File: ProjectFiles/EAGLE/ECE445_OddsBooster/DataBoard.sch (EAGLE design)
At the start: 52 parts, among them U2 74LV164D-SHIFT_REGISTER, U3 74LV164D-SHIFT_REGISTER, U4 74LV164D-SHIFT_REGISTER, X1 FH12-40S-0.5SH

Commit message: footprints, schematic building, component checks
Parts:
- removed C10: 150u, rcl:C-USC0805
- removed C2: 68u, rcl:C-USC0805
- removed C9, CSP, C_IN: 0.1u, rcl:C-USC0805
- removed CFB: 180p, rcl:C-USC0805
- removed CZ: 0.01u, rcl:C-USC0805
- removed C_OUT: 10u, rcl:C-USC0805
- removed D2: DB2X20700L-DIODE, OddsBooster:DB2X20700L-DIODE
- removed JP2: USB-B Micro, pinhead:PINHD-1X5
- removed JP3: (no value), pinhead:PINHD-1X3
- removed L: 10u, rcl:L-USL1812
- removed LP3965-ADJ: (no value), pinhead:PINHD-1X5
- removed MIC2169: (no value), pinhead:PINHD-2X5
- removed R11: 560, rcl:R-US_R0805
- removed R12, RFB2: 8.2k, rcl:R-US_R0805
- removed R13: 1.5k, rcl:R-US_R0805
- removed R14: 1k, pot:TRIM_US-3223G
- removed R15: 2k, pot:TRIM_US-SM-42/43B
- removed RDUTY: 240k, rcl:R-US_R0805
- removed RFB1: 82k, rcl:R-US_R0805
- removed ROSC: 280k, rcl:R-US_R0805
- removed RZ: 200k, rcl:R-US_R0805
- removed S-8337ABIA-T8T1U: (no value), pinhead:PINHD-2X4
- added BSH, DMG1, DMG2: DMG2302UQ-AND-BSH105-NMOS, OddsBooster:DMG2302UQ-AND-BSH105-NMOS
- added C13: 100p, rcl:C-USC0805
- added C14, CSP1, C_IN1: 0.1u, rcl:C-USC0805
- added C16: 100u, rcl:C-USC1210
- added CFB1: 180p, rcl:C-USC0805
- added CZ1: 0.01u, rcl:C-USC0805
- added C_OUT1: 10u, rcl:C-USC0805
- added D4: DB2X20700L-DIODE, OddsBooster:DB2X20700L-DIODE
- added JP4: USB-B Micro, pinhead:PINHD-1X5
- added JP5: (no value), pinhead:PINHD-1X3
- added L2: 10u, OddsBooster:SRP0415-BOURNS-100K-10U
- added R16, R19: 10k, rcl:R-US_R0805
- added R17, R18: 33k, rcl:R-US_R0805
- added R20: 2k, pot:TRIM_US-3223G
- added RDUTY1: 240k, rcl:R-US_R0805
- added RFB3: 82k, rcl:R-US_R0805
- added RFB4: 8.2k, rcl:R-US_R0805
- added ROSC1: 280k, rcl:R-US_R0805
- added RZ1: 200k, rcl:R-US_R0805
- added U5: LP3965-ADJ-LDO, OddsBooster:LP3965-ADJ-LDO
- added U6: MIC2169-BUCK, OddsBooster:MIC2169-BUCK
- added U7: S-8337ABIA-T8T1U-BOOSTCONVERTER, OddsBooster:S-8337ABIA-T8T1U-BOOSTCONVERTER
- added X2: XH-BAT-CONN, OddsBooster:XH-BAT-CONN
- C3: value 33u -> 150p
- C4: value 100p -> 0.1p; device rcl:C-USC0805 -> rcl:C-USC0603
- C5: value 0.1p -> 68u; device rcl:C-USC0805 -> rcl:C-USC1206
- C6: value 150p -> 33u; device rcl:C-USC0805 -> OddsBooster:NEMCO-33U-TANT-CAP
- C7: value 4.7u -> 150u; device rcl:C-USC0805 -> OddsBooster:KEMET-T491-150U-TANT
- C8: value 100u -> 4.7u; device rcl:C-USC1210 -> rcl:C-USC0603
- D1: value Diode -> SL34A-DIODE; device diode:1N821 -> OddsBooster:SL34A-DIODE
- L1: value 3.3u -> SRP0415-BOURNS-100K-10U; device rcl:L-USL2825P -> OddsBooster:SRP0415-BOURNS-100K-10U
- R10: value 2 -> 1k; device rcl:R-US_R0805 -> OddsBooster:BOURNS-3316P-2KPOT
- R4: value 10k -> 4k
- R5: value 33k -> 2
- R6: value 33k -> 560
- R7: value 10k -> 8.2k
- R8: value 2k -> 1.5k; device pot:TRIM_US-3223G -> rcl:R-US_R0805
- R9: value 4k -> BOURNS-3316P-2KPOT; device rcl:R-US_R0805 -> OddsBooster:BOURNS-3316P-2KPOT
- X1: value FH12-40S-0.5SH -> FH40-40S-HIROSE-FPC; device con-hirose:FH12-40S-0.5SH -> OddsBooster:FH40-40S-HIROSE-FPC
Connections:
- removed net N$10: MIC2169.5, R11.1
- removed net N$11: C9.1, D1.C, MIC2169.2
- removed net N$12: C5.1, C6.1, MIC2169.7
- removed net N$13: MIC2169.9, R12.1, R13.2
- removed net N$14: R13.1, R14.E
- removed net N$15: D2.P$1, L.2
- removed net N$16: CSP.1, S-8337ABIA-T8T1U.5
- removed net N$17: S-8337ABIA-T8T1U.8
- removed net N$19: CZ.1, RZ.1
- removed net N$20: RZ.2, S-8337ABIA-T8T1U.1
- removed net N$21: CFB.2, RFB1.1, RFB2.2, S-8337ABIA-T8T1U.3
- removed net N$22: ROSC.2, S-8337ABIA-T8T1U.4
- removed net N$23: RDUTY.2, S-8337ABIA-T8T1U.2
- removed net N$24: R15.E, RFB2.1
- removed net N$4: C9.2, L1.1, R10.2
- removed net N$5: MIC2169.8
- removed net N$6: MIC2169.6, R10.1
- removed net N$7: MIC2169.4
- removed net N$8: LP3965-ADJ.1, R7.2
- removed net N$9: C5.2, R9.2
- removed net UART_3V3: JP1.1, U1.3V3
- removed net UART_GND: JP1.2, U1.GND38
- new net N$18: C13.2, R16.2, R17.1, R18.1, U5.ADJ
- new net N$25: R19.2, U5.SD
- new net N$26: R17.2, R18.2, R20.A
- new net N$27: DMG1.G, U6.HSD
- new net N$28: DMG2.G, U6.LSD
- new net N$29: R6.1, U6.CS
- new net N$30: C4.2, R4.2
- new net N$31: C3.1, C4.1, U6.COMP
- new net N$32: C14.1, D1.C
- new net N$33: R7.1, R8.2, U6.FB
- new net N$34: R10.P$1, R8.1
- new net N$35: CSP1.1, U7.CSP
- new net N$36: BSH.G, U7.EX
- new net N$37: CZ1.1, RZ1.1
- new net N$38: RZ1.2, U7.CC
- new net N$39: CFB1.2, RFB3.1, RFB4.2, U7.FB
- new net N$40: ROSC1.2, U7.ROSC
- new net N$41: RDUTY1.2, U7.RDUTY-ON/OFF
- new net N$42: R9.P$1, RFB4.1
- new net N$43: BSH.D, D4.P$1, L1.P$2
- new net V_IN: C5.1, C_IN1.1, JP5.3, L1.P$1, R19.1, U5.VIN, U7.VIN
- net B0: now also X1.P$21; no longer X1-21.1
- net B1: now also X1.P$22; no longer X1-22.1
- net B2: now also X1.P$23; no longer X1-23.1
- net B3: now also X1.P$24; no longer X1-24.1
- net B4: now also X1.P$25; no longer X1-25.1
- net B5: now also X1.P$26; no longer X1-26.1
- net B6: now also X1.P$27; no longer X1-27.1
- net B7: now also X1.P$28; no longer X1-28.1
- net CLK_6.5: now also X1.P$30; no longer X1-30.1
- net DE: now also X1.P$34; no longer X1-34.1
- net G0: now also X1.P$13; no longer X1-13.1
- net G1: now also X1.P$14; no longer X1-14.1
- net G2: now also X1.P$15; no longer X1-15.1
- net G3: now also X1.P$16; no longer X1-16.1
- net G4: now also X1.P$17; no longer X1-17.1
- net G5: now also X1.P$18; no longer X1-18.1
- net G6: now also X1.P$19; no longer X1-19.1
- net G7: now also X1.P$20; no longer X1-20.1
- net GND: now also BSH.S, C16.2, C5.2, C6.P$1, C7.P$2, CSP1.2, CZ1.2, C_IN1.2, C_OUT1.2, DMG2.S, JP1.2, JP4.5, R10.P$2, R10.P$3, R16.1, R9.P$2, R9.P$3, RDUTY1.1, ROSC1.1, U1.GND38, U5.GND, U6.GND, U7.VSS, X1.P$2, X1.P$29, X2.P$2; no longer C10.2, C2.2, C6.2, C7.2, CSP.2, CZ.2, C_IN.2, C_OUT.2, JP2.5, LP3965-ADJ.3, MIC2169.10, R14.A, R15.S, R7.1, R9.1, RDUTY.1, ROSC.1, S-8337ABIA-T8T1U.6, X1-2.1, X1-29.1
- net HSYNC: now also X1.P$32; no longer X1-32.1
- net N$1: now also C14.2, DMG1.S, DMG2.D, L2.P$1, R5.2; no longer C7.1, D1.A, MIC2169.3
- net N$2: now also C8.1, D1.A, U6.BST, U6.VDD; no longer R5.2, R6.2, R8.A
- net N$3: now also U6.VSW; no longer C4.2, LP3965-ADJ.5, R4.2, R6.1
- net R0: now also X1.P$5; no longer X1-5.1
- net R1: now also X1.P$6; no longer X1-6.1
- net R2: now also X1.P$7; no longer X1-7.1
- net R3: now also X1.P$8; no longer X1-8.1
- net R4: now also X1.P$9; no longer X1-9.1
- net R5: now also X1.P$10; no longer X1-10.1
- net R6: now also X1.P$11; no longer X1-11.1
- net R7: now also X1.P$12; no longer X1-12.1
- net VCC: now also C13.1, C6.P$2, JP1.1, R20.S, U1.3V3, U5.VOUT, X1.P$31, X1.P$4; no longer C3.1, C4.1, LP3965-ADJ.4, R8.S, X1-31.1, X1-4.1
- net VDD: now also CFB1.1, C_OUT1.1, D4.P$2, RFB3.2, X1.P$1; no longer CFB.1, C_OUT.1, D2.P$2, RFB1.2, X1-1.1
- net VSYNC: now also X1.P$33; no longer X1-33.1
- net V_BAT: now also JP5.2, X2.P$1; no longer C2.1, C_IN.1, L.1, LP3965-ADJ.2, S-8337ABIA-T8T1U.7
- net V_CHARGE: now also C7.P$1, JP5.1, L2.P$2, R7.2; no longer C10.1, L1.2, R12.2
- net V_USB: now also C16.1, DMG1.D, JP4.1, R6.2, U6.VIN; no longer C8.1, JP2.1, MIC2169.1, R11.2
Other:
- note added: "3-way Switch"
- note added: "Power Subsystem Boost Converter"
- note added: "Power Subsystem Buck Converter"
- note added: "Power Subsystem LDO Linear Voltage Regulator"
- note added: "UART_3V3"
- note added: "UART_GND"
- note removed: "LCD"
- moved on the sheet: C1, C3, C4, C5, C8, JP1, R1, R2, R3, R4, R5, R6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

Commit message: eagle updates
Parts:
- added AE1: W3102-ANTENNA, OddsBooster_3_8_6PM:W3102-ANTENNA
- added C10, C15, C21: 15pF, rcl:C-USC0805K
- added C11, C17, C18, C19: 68pF, rcl:C-USC0805K
- added C12: 0.22uF, rcl:C-USC0402
- added C2: 4.7uF, OddsBooster_3_8_6PM:865080640004-ELECTROLYTIC-CAP
- added C20: 8.2pF, rcl:C-USC0402
- added C22, C9: 0.1uF, rcl:C-USC0805
- added L3, L4: 0.1uF, OddsBooster_3_8_6PM:SRP0415-BOURNS-100K-10U
- added R11: 10k, rcl:R-US_R0805
- added R12: 820, rcl:R-US_R0805
- added R13: 2.7k, rcl:R-US_R0805
- added U8: MFRC500, OddsBooster_3_8_6PM:MFRC500
- added X3: CFPX-180-XTAL-OSCILLATOR, OddsBooster_3_8_6PM:CFPX-180-XTAL-OSCILLATOR
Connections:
- removed net N$32: C14.1, D1.C
- new net 0: C10.1, C11.2, C12.2, C15.1, C17.1, C18.2, C19.1, C2.2, C22.2, C9.2, R11.2, U8.A2, U8.AVSS, U8.DVSS, U8.MFIN, U8.NCS, U8.TVSS
- new net N$10: C21.1, R13.1
- new net N$11: L3.P$2, U8.TX1
- new net N$12: L4.P$2, U8.TX2
- new net N$13: AE1.1, C11.1, C18.1, C20.2, C21.2, L3.P$1
- new net N$14: AE1.P$1, C17.2, C19.2, C20.1, L4.P$1
- new net N$4: C14.1, D1.C, U6.BST
- new net N$5: C10.2, U8.OSCIN, X3.1
- new net N$6: C15.2, U8.OSCOUT, X3.2
- new net N$7: R11.1, U8.RSTPD
- new net N$8: C9.1, R12.1, U8.VMID
- new net N$9: R12.2, R13.2, U8.RX
- net ALE: now also U8.ALE
- net D0: now also U8.D0
- net D1: now also U8.D1
- net D2: now also U8.D2
- net D3: now also U8.D3
- net D4: now also U8.D4
- net D5: now also U8.D5
- net D6: now also U8.D6
- net D7: now also U8.D7
- net GND: now also U1.GND40, U1.GND41, U1.GND42, U1.GND43, U1.GND44, U1.GND45, U1.GND46, U1.GND47
- net IRQ: now also U8.IRQ
- net N$2: no longer U6.BST
- net NRD: now also U8.NRD
- net NWR: now also U8.NWR
- net VCC: now also C12.1, C2.1, C22.1, U8.A0/NWAIT, U8.A1, U8.AVDD, U8.DVDD, U8.TVDD
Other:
- moved on the sheet: C14, D1, R5

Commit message: PCB done along with generated gerber files
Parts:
- C2: device OddsBooster_3_8_6PM:865080640004-ELECTROLYTIC-CAP -> OddsBooster:865080640004-ELECTROLYTIC-CAP
- X3: device OddsBooster_3_8_6PM:CFPX-180-XTAL-OSCILLATOR -> OddsBooster:CFPX-180-XTAL-OSCILLATOR
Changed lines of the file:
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@@
 <part name="AE1" library="OddsBooster_3_8_6PM" deviceset="W3102-ANTENNA" device=""/>
 <part name="U8" library="OddsBooster_3_8_6PM" deviceset="MFRC500" device=""/>
-<part name="C2" library="OddsBooster_3_8_6PM" deviceset="865080640004-ELECTROLYTIC-CAP" device="" value="4.7uF"/>
+<part name="C2" library="OddsBooster" deviceset="865080640004-ELECTROLYTIC-CAP" device="" value="4.7uF"/>
 <part name="L3" library="OddsBooster_3_8_6PM" deviceset="SRP0415-BOURNS-100K-10U" device="" value="0.1uF"/>
 <part name="C9" library="rcl" library_urn="urn:adsk.eagle:library:334" deviceset="C-US" device="C0805" package3d_urn="urn:adsk.eagle:package:23617/2" value="0.1uF"/>
@@
 <part name="R13" library="rcl" library_urn="urn:adsk.eagle:library:334" deviceset="R-US_" device="R0805" package3d_urn="urn:adsk.eagle:package:23553/2" value="2.7k"/>
 <part name="C12" library="rcl" library_urn="urn:adsk.eagle:library:334" deviceset="C-US" device="C0402" package3d_urn="urn:adsk.eagle:package:23626/2" value="0.22uF"/>
-<part name="X3" library="OddsBooster_3_8_6PM" deviceset="CFPX-180-XTAL-OSCILLATOR" device=""/>
+<part name="X3" library="OddsBooster" deviceset="CFPX-180-XTAL-OSCILLATOR" device=""/>
 <part name="C15" library="rcl" library_urn="urn:adsk.eagle:library:334" deviceset="C-US" device="C0805K" package3d_urn="urn:adsk.eagle:package:23681/2" value="15pF"/>
 <part name="X_1" library="ngspice-simulation" library_urn="urn:adsk.eagle:library:527439" deviceset="GND" device=""/>

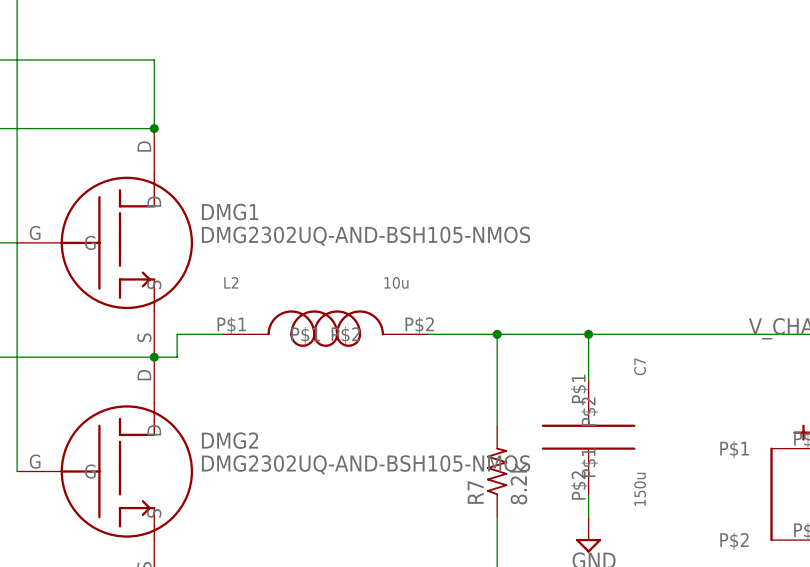
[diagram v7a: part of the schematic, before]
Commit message: working bluetooth mcu firmware, flash-able lcd mcu firmware, working bluetooth app debug and connection window
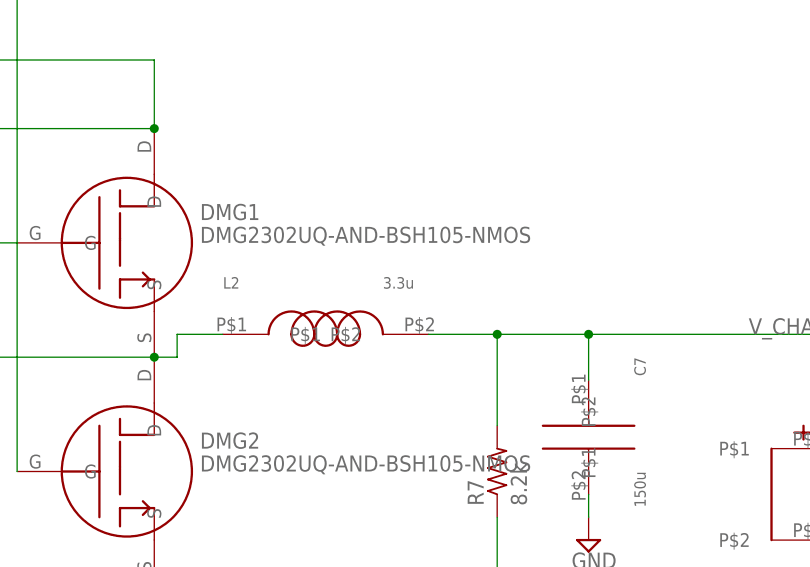
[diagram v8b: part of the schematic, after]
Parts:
- L2: value 10u -> 3.3u
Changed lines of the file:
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@@
 <part name="DMG1" library="OddsBooster" deviceset="DMG2302UQ-AND-BSH105-NMOS" device=""/>
 <part name="DMG2" library="OddsBooster" deviceset="DMG2302UQ-AND-BSH105-NMOS" device=""/>
-<part name="L2" library="OddsBooster" deviceset="SRP0415-BOURNS-100K-10U" device="" value="10u"/>
+<part name="L2" library="OddsBooster" deviceset="SRP0415-BOURNS-100K-10U" device="" value="3.3u"/>
 <part name="C7" library="OddsBooster" deviceset="KEMET-T491-150U-TANT" device="" value="150u"/>
 <part name="C8" library="rcl" library_urn="urn:adsk.eagle:library:334" deviceset="C-US" device="C0603" package3d_urn="urn:adsk.eagle:package:23616/2" value="4.7u"/>
